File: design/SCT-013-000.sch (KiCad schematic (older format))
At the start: 2 parts, among them U1 sj-3503-smt

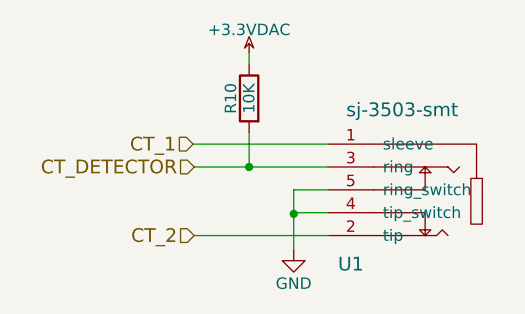
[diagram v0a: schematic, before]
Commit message: Starting PIVI 2.0 * sch ready. * components in PCB placed.
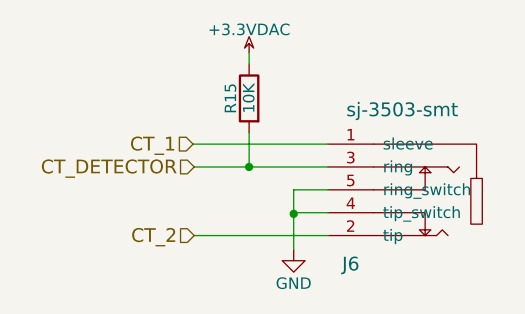
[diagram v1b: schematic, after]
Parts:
- J2: renamed from U1; footprint (none) -> LESS:SJ-3503-SMT
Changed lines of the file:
@@
 $Descr A4 11693 8268
 encoding utf-8
-Sheet 4 20
+Sheet 9 20
 Title "PIVI"
 Date "Mon 27 Jul 2015"
@@
 	4920 3925 5505 3925
 $Comp
-L GND #PWR35
+L GND #PWR039
 U 1 1 55B1DDA9
 P 5355 3985
-AR Path="/549598FF/55B37AF3/55B1DDA9" Ref="#PWR35"  Part="1"
-AR Path="/549598FF/55B659F5/55B1DDA9" Ref="#PWR33"  Part="1"
-AR Path="/549598FF/55B38046/55B1DDA9" Ref="#PWR37"  Part="1"
-AR Path="/549598FF/55B38E62/55B1DDA9" Ref="#PWR39"  Part="1"
-AR Path="/549598FF/55B38E6D/55B1DDA9" Ref="#PWR41"  Part="1"
-AR Path="/549598FF/55B38E78/55B1DDA9" Ref="#PWR43"  Part="1"
-F 0 "#PWR33" H 5355 3735 50  0001 C CNN
+AR Path="/549598FF/55B37AF3/55B1DDA9" Ref="#PWR039"  Part="1"
+AR Path="/549598FF/55B659F5/55B1DDA9" Ref="#PWR037"  Part="1"
+AR Path="/549598FF/55B38046/55B1DDA9" Ref="#PWR041"  Part="1"
+AR Path="/549598FF/55B38E62/55B1DDA9" Ref="#PWR043"  Part="1"
+AR Path="/549598FF/55B38E6D/55B1DDA9" Ref="#PWR045"  Part="1"
+AR Path="/549598FF/55B38E78/55B1DDA9" Ref="#PWR047"  Part="1"
+F 0 "#PWR047" H 5355 3735 50  0001 C CNN
 F 1 "GND" H 5355 3835 50  0000 C CNN
 F 2 "" H 5355 3985 60  0000 C CNN
@@
 AR Path="/549598FF/55B38E6D/55B1DDFF" Ref="R14"  Part="1"
 AR Path="/549598FF/55B38E78/55B1DDFF" Ref="R15"  Part="1"
-F 0 "R10" V 5240 3325 50  0000 C CNN
+F 0 "R15" V 5240 3325 50  0000 C CNN
 F 1 "10K" V 5160 3325 50  0000 C CNN
 F 2 "Resistors_SMD:R_0603" V 5090 3325 30  0001 C CNN
@@
 Connection ~ 5355 3830
 $Comp
-L +3.3VDAC #PWR34
+L +3.3VDAC #PWR040
 U 1 1 55BEA320
 P 5160 3125
-AR Path="/549598FF/55B37AF3/55BEA320" Ref="#PWR34"  Part="1"
-AR Path="/549598FF/55B659F5/55BEA320" Ref="#PWR32"  Part="1"
-AR Path="/549598FF/55B38046/55BEA320" Ref="#PWR36"  Part="1"
-AR Path="/549598FF/55B38E62/55BEA320" Ref="#PWR38"  Part="1"
-AR Path="/549598FF/55B38E6D/55BEA320" Ref="#PWR40"  Part="1"
-AR Path="/549598FF/55B38E78/55BEA320" Ref="#PWR42"  Part="1"
-F 0 "#PWR32" H 5310 3075 50  0001 C CNN
+AR Path="/549598FF/55B37AF3/55BEA320" Ref="#PWR040"  Part="1"
+AR Path="/549598FF/55B659F5/55BEA320" Ref="#PWR038"  Part="1"
+AR Path="/549598FF/55B38046/55BEA320" Ref="#PWR042"  Part="1"
+AR Path="/549598FF/55B38E62/55BEA320" Ref="#PWR044"  Part="1"
+AR Path="/549598FF/55B38E6D/55BEA320" Ref="#PWR046"  Part="1"
+AR Path="/549598FF/55B38E78/55BEA320" Ref="#PWR048"  Part="1"
+F 0 "#PWR048" H 5310 3075 50  0001 C CNN
 F 1 "+3.3VDAC" H 5160 3225 50  0000 C CNN
 F 2 "" H 5160 3125 60  0000 C CNN
@@
 $EndComp
 $Comp
-L sj-3503-smt U1
+L sj-3503-smt J2
 U 1 1 55BF1B7D
 P 5680 3625
-AR Path="/549598FF/55B37AF3/55BF1B7D" Ref="U1"  Part="1"
-AR Path="/549598FF/55B659F5/55BF1B7D" Ref="U1"  Part="1"
-AR Path="/549598FF/55B38046/55BF1B7D" Ref="U1"  Part="1"
-AR Path="/549598FF/55B38E62/55BF1B7D" Ref="U1"  Part="1"
-AR Path="/549598FF/55B38E6D/55BF1B7D" Ref="U1"  Part="1"
-AR Path="/549598FF/55B38E78/55BF1B7D" Ref="U2"  Part="1"
-F 0 "U1" H 5605 3200 60  0000 C CNN
+AR Path="/549598FF/55B37AF3/55BF1B7D" Ref="J2"  Part="1"
+AR Path="/549598FF/55B659F5/55BF1B7D" Ref="J1"  Part="1"
+AR Path="/549598FF/55B38046/55BF1B7D" Ref="J3"  Part="1"
+AR Path="/549598FF/55B38E62/55BF1B7D" Ref="J4"  Part="1"
+AR Path="/549598FF/55B38E6D/55BF1B7D" Ref="J5"  Part="1"
+AR Path="/549598FF/55B38E78/55BF1B7D" Ref="J6"  Part="1"
+F 0 "J6" H 5605 3200 60  0000 C CNN
 F 1 "sj-3503-smt" H 5830 3875 60  0000 C CNN
-F 2 "" H 5680 3625 60  0000 C CNN
+F 2 "LESS:SJ-3503-SMT" H 5680 3625 60  0001 C CNN
 F 3 "" H 5680 3625 60  0000 C CNN
 	1    5680 3625

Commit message: PCB routed + BOM complete
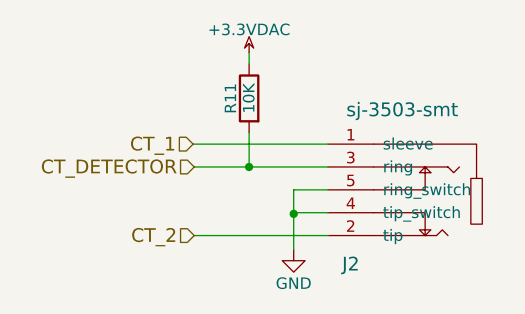
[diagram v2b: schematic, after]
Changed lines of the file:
@@
 AR Path="/549598FF/55B38E6D/55B1DDFF" Ref="R14"  Part="1"
 AR Path="/549598FF/55B38E78/55B1DDFF" Ref="R15"  Part="1"
-F 0 "R15" V 5240 3325 50  0000 C CNN
+F 0 "R11" V 5240 3325 50  0000 C CNN
 F 1 "10K" V 5160 3325 50  0000 C CNN
 F 2 "Resistors_SMD:R_0603" V 5090 3325 30  0001 C CNN
@@
 AR Path="/549598FF/55B38E6D/55BF1B7D" Ref="J5"  Part="1"
 AR Path="/549598FF/55B38E78/55BF1B7D" Ref="J6"  Part="1"
-F 0 "J6" H 5605 3200 60  0000 C CNN
+F 0 "J2" H 5605 3200 60  0000 C CNN
 F 1 "sj-3503-smt" H 5830 3875 60  0000 C CNN
 F 2 "LESS:SJ-3503-SMT" H 5680 3625 60  0001 C CNN

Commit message: Fix #10: main route not connected.
Right now we have the following power labels:
* +5V from 220v to Raspberry pi and voltage regulator.
* +3V3 from voltage regulator to microcontroller imput and measurement voltage circuit.
* +3.3VP DC digital +3.3v (filter to MCU).
* +3.3VADC DC analog +3.3v
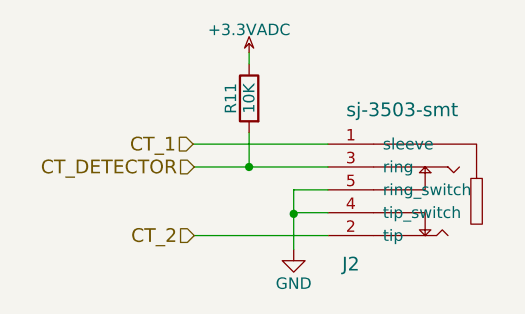
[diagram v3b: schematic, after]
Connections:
- net +3.3VDAC renamed +3.3VADC
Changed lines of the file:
@@
 LIBS:txs0104e
 LIBS:less
-LIBS:pivi-shield-cache
 EELAYER 25 0
 EELAYER END
 $Descr A4 11693 8268
 encoding utf-8
-Sheet 9 20
+Sheet 5 20
 Title "PIVI"
 Date "Mon 27 Jul 2015"
@@
 	4920 3925 5505 3925
 $Comp
-L GND #PWR039
+L GND #PWR041
 U 1 1 55B1DDA9
 P 5355 3985
-AR Path="/549598FF/55B37AF3/55B1DDA9" Ref="#PWR039"  Part="1"
-AR Path="/549598FF/55B659F5/55B1DDA9" Ref="#PWR037"  Part="1"
-AR Path="/549598FF/55B38046/55B1DDA9" Ref="#PWR041"  Part="1"
-AR Path="/549598FF/55B38E62/55B1DDA9" Ref="#PWR043"  Part="1"
-AR Path="/549598FF/55B38E6D/55B1DDA9" Ref="#PWR045"  Part="1"
-AR Path="/549598FF/55B38E78/55B1DDA9" Ref="#PWR047"  Part="1"
-F 0 "#PWR047" H 5355 3735 50  0001 C CNN
+AR Path="/549598FF/55B37AF3/55B1DDA9" Ref="#PWR041"  Part="1"
+AR Path="/549598FF/55B659F5/55B1DDA9" Ref="#PWR039"  Part="1"
+AR Path="/549598FF/55B38046/55B1DDA9" Ref="#PWR043"  Part="1"
+AR Path="/549598FF/55B38E62/55B1DDA9" Ref="#PWR045"  Part="1"
+AR Path="/549598FF/55B38E6D/55B1DDA9" Ref="#PWR047"  Part="1"
+AR Path="/549598FF/55B38E78/55B1DDA9" Ref="#PWR049"  Part="1"
+F 0 "#PWR049" H 5355 3735 50  0001 C CNN
 F 1 "GND" H 5355 3835 50  0000 C CNN
 F 2 "" H 5355 3985 60  0000 C CNN
@@
 Connection ~ 5355 3830
 $Comp
-L +3.3VDAC #PWR040
-U 1 1 55BEA320
-P 5160 3125
-AR Path="/549598FF/55B37AF3/55BEA320" Ref="#PWR040"  Part="1"
-AR Path="/549598FF/55B659F5/55BEA320" Ref="#PWR038"  Part="1"
-AR Path="/549598FF/55B38046/55BEA320" Ref="#PWR042"  Part="1"
-AR Path="/549598FF/55B38E62/55BEA320" Ref="#PWR044"  Part="1"
-AR Path="/549598FF/55B38E6D/55BEA320" Ref="#PWR046"  Part="1"
-AR Path="/549598FF/55B38E78/55BEA320" Ref="#PWR048"  Part="1"
-F 0 "#PWR048" H 5310 3075 50  0001 C CNN
-F 1 "+3.3VDAC" H 5160 3225 50  0000 C CNN
-F 2 "" H 5160 3125 60  0000 C CNN
-F 3 "" H 5160 3125 60  0000 C CNN
-	1    5160 3125
-	1    0    0    -1
-$EndComp
-$Comp
 L sj-3503-smt J2
 U 1 1 55BF1B7D
@@
 	1    0    0    -1
 $EndComp
+$Comp
+L +3.3VADC #PWR040
+U 1 1 55F58901
+P 5160 3125
+AR Path="/549598FF/55B659F5/55F58901" Ref="#PWR040"  Part="1"
+AR Path="/549598FF/55B37AF3/55F58901" Ref="#PWR042"  Part="1"
+AR Path="/549598FF/55B38046/55F58901" Ref="#PWR044"  Part="1"
+AR Path="/549598FF/55B38E62/55F58901" Ref="#PWR046"  Part="1"
+AR Path="/549598FF/55B38E6D/55F58901" Ref="#PWR048"  Part="1"
+AR Path="/549598FF/55B38E78/55F58901" Ref="#PWR050"  Part="1"
+F 0 "#PWR050" H 5310 3075 50  0001 C CNN
+F 1 "+3.3VADC" H 5160 3225 50  0000 C CNN
+F 2 "" H 5160 3125 60  0000 C CNN
+F 3 "" H 5160 3125 60  0000 C CNN
+	1    5160 3125
+	1    0    0    -1
+$EndComp

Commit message: Fix #7, Fix #8, Fix #9, Fix #10, Fix #11
Several fixes improvements:
* Fix #7: Add 2mm idle to each side of the connector.
* Fix #8: Add 0.25mm to each side of the connector.
* Fix #9: Mirror component. Checked with the datasheet.
* Fix #10: correct label name.
* Fix #11: Changed the terminal block for one with a better mouting system.

Also check the Raspberry pi 20 pin header. It is place in the correct position.
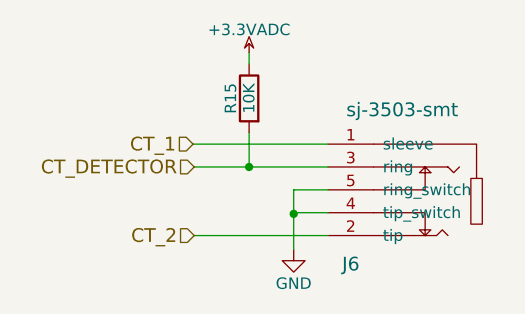
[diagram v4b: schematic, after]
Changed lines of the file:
@@
 AR Path="/549598FF/55B38E6D/55B1DDFF" Ref="R14"  Part="1"
 AR Path="/549598FF/55B38E78/55B1DDFF" Ref="R15"  Part="1"
-F 0 "R11" V 5240 3325 50  0000 C CNN
+F 0 "R15" V 5240 3325 50  0000 C CNN
 F 1 "10K" V 5160 3325 50  0000 C CNN
 F 2 "Resistors_SMD:R_0603" V 5090 3325 30  0001 C CNN
@@
 AR Path="/549598FF/55B38E6D/55BF1B7D" Ref="J5"  Part="1"
 AR Path="/549598FF/55B38E78/55BF1B7D" Ref="J6"  Part="1"
-F 0 "J2" H 5605 3200 60  0000 C CNN
+F 0 "J6" H 5605 3200 60  0000 C CNN
 F 1 "sj-3503-smt" H 5830 3875 60  0000 C CNN
 F 2 "LESS:SJ-3503-SMT" H 5680 3625 60  0001 C CNN
